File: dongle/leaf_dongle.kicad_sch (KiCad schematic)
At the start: 7 parts, among them J1 UP20-C-F-G-FL-P12-TR

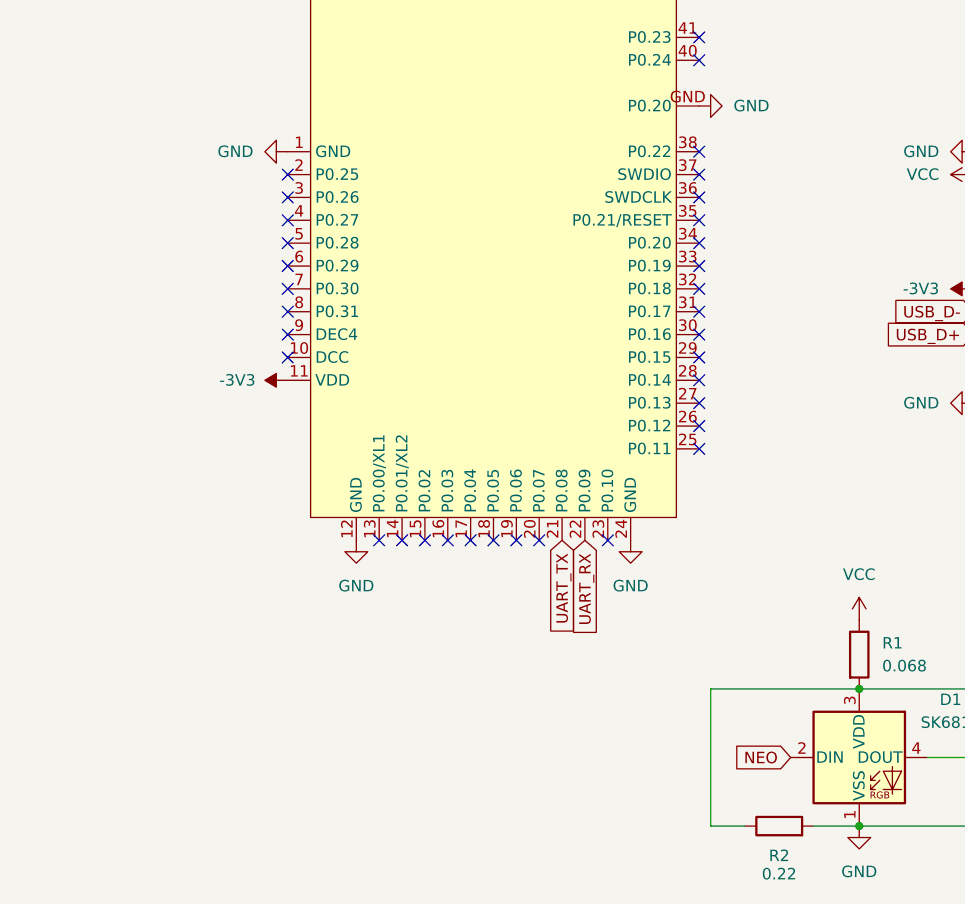
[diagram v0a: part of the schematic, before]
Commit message: Add TC-2030 interface; generate gerbers
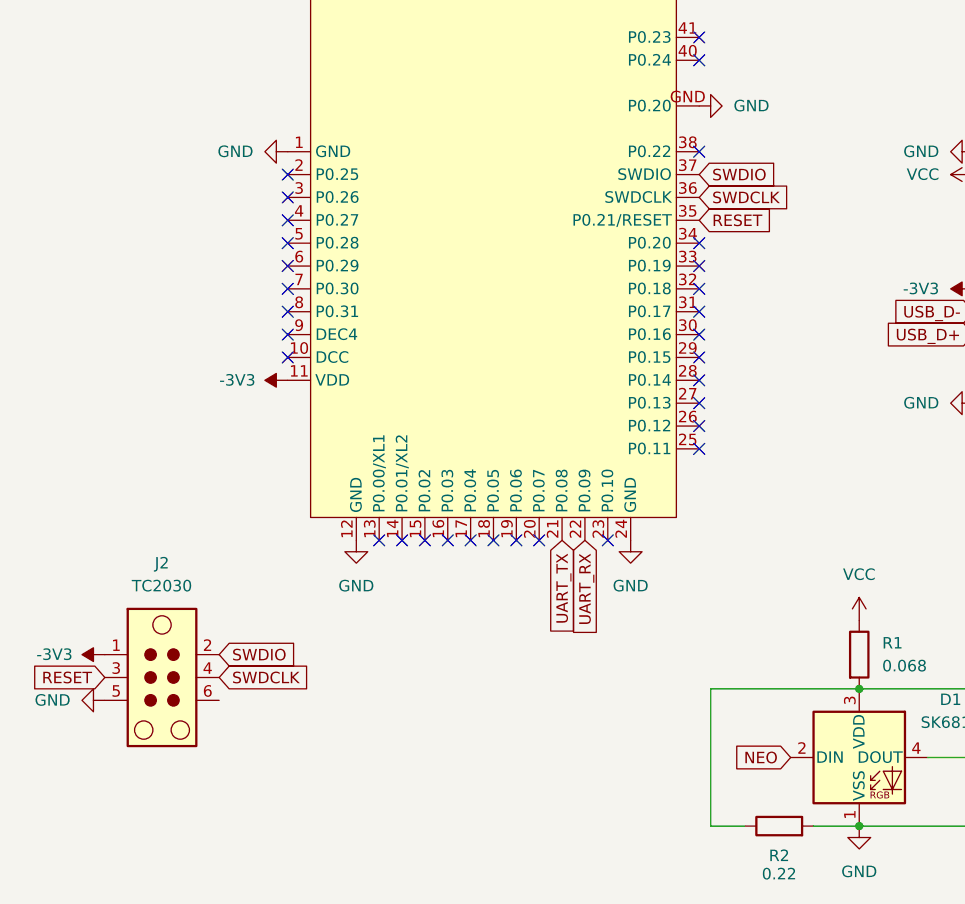
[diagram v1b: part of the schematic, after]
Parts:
- added J2: TC2030, Connector:Tag-Connect_TC2030-IDC-NL_2x03_P1.27mm_Vertical, symbol Connector:TC2030
- 1, U1: value ~ -> (none)
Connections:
- net -3V3: now also J2.1
- net GND: now also J2.5
- net RESET: now reaches U1.35 (P0.21/RESET)
- net RESET: now also J2.3
- net SWDCLK: now reaches U1.36 (SWDCLK)
- net SWDCLK: now also J2.4
- net SWDIO: now reaches U1.37 (SWDIO)
- net SWDIO: now also J2.2
- no-connect marks 63 -> 60

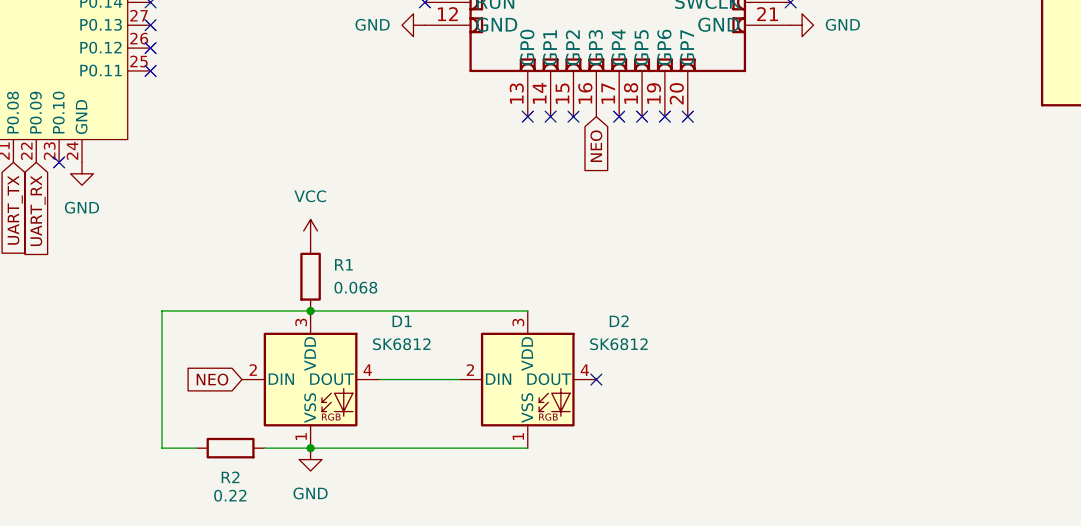
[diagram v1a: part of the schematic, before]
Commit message: Use logic shifter on dongle
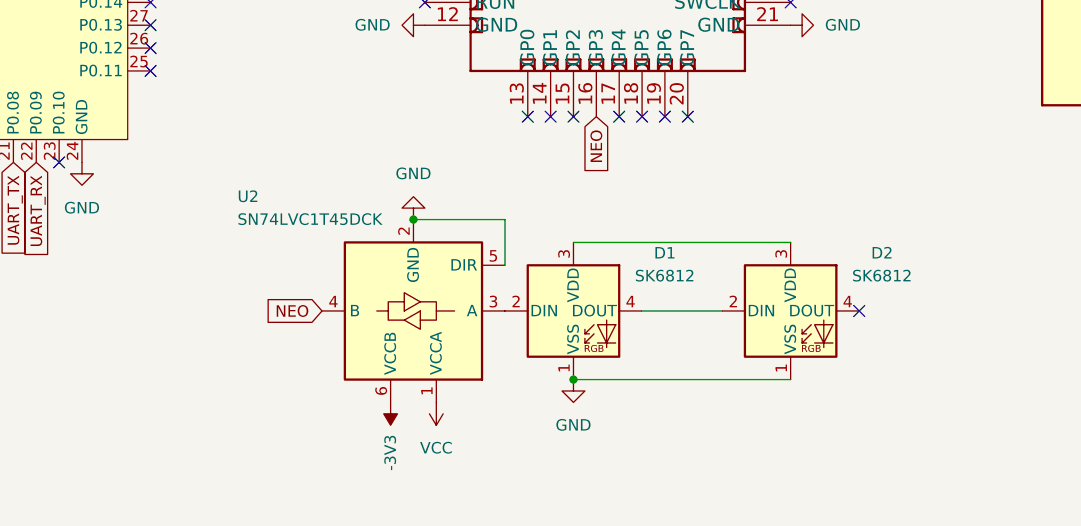
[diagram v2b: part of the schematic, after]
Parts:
- removed R1: 0.068, Resistor_SMD:R_0805_2012Metric, symbol Device:R
- removed R2: 0.22, Resistor_SMD:R_0805_2012Metric, symbol Device:R
- added U2: SN74LVC1T45DCK, Package_TO_SOT_SMD:SOT-363_SC-70-6, symbol Logic_LevelTranslator:SN74LVC1T45DCK
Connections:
- net -3V3: now also U2.6 (VCCB)
- net GND: now also U2.2 (GND), U2.5 (DIR)
- net NEO: now also U2.4 (B); no longer D1.2 (DIN)
- net VCC: now also U2.1 (VCCA)
- new net: D1.2 (DIN), U2.3 (A)
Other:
- moved on the sheet: D1, D2

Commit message: Update dongle to have 5.1k resistor for USB power
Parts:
- added R1: 5.1k, Resistor_SMD:R_0402_1005Metric, symbol Device:R
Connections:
- net GND: now also R1.2
- net at J1.A5 (CC1): now also R1.1
- no-connect marks 60 -> 59
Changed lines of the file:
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@@
 	)
 	(no_connect
-		(at 243.84 92.71)
-	)
-	(no_connect
 		(at 243.84 107.95)
 	)
@@
 	)
 	(symbol
+		(lib_id "Device:R")
+		(at 247.65 92.71 90)
+		(unit 1)
+		(body_style 1)
+		(exclude_from_sim no)
+		(in_bom yes)
+		(on_board yes)
+		(in_pos_files yes)
+		(dnp no)
+		(property "Reference" "R1"
+			(at 251.206 90.424 90)
+			(show_name no)
+			(do_not_autoplace no)
+			(effects
+				(font
+					(size 1.27 1.27)
+				)
+			)
+		)
+		(property "Value" "5.1k"
+			(at 255.524 90.424 90)
+			(show_name no)
+			(do_not_autoplace no)
+			(effects
+				(font
+					(size 1.27 1.27)
+				)
+			)
+		)
+		(property "Footprint" "Resistor_SMD:R_0402_1005Metric"
+			(at 247.65 94.488 90)
+			(hide yes)
+			(show_name no)
+			(do_not_autoplace no)
+			(effects
+				(font
+					(size 1.27 1.27)
+				)
+			)
+		)
+		(property "Datasheet" ""
+			(at 247.65 92.71 0)
+			(hide yes)
+			(show_name no)
+			(do_not_autoplace no)
+			(effects
+				(font
+					(size 1.27 1.27)
+				)
+			)
+		)
+		(property "Description" "Resistor"
+			(at 247.65 92.71 0)
+			(hide yes)
+			(show_name no)
+			(do_not_autoplace no)
+			(effects
+				(font
+					(size 1.27 1.27)
+				)
+			)
+		)
+		(pin "1"
+		)
+		(pin "2"
+		)
+		(instances
+			(project "leaf_dongle"
+				(path "/f6de454d-ae1c-4e0e-a2ba-a5d84f7bcb5c"
+					(reference "R1")
+					(unit 1)
+				)
+			)
+		)
+	)
+	(symbol
 		(lib_id "power:-3V3")
 		(at 58.42 132.08 90)
@@
 					(unit 1)
 				)
+			)
+		)
+	)
+	(symbol
+		(lib_id "power:GND")
+		(at 251.46 92.71 90)
+		(unit 1)
+		(body_style 1)
+		(exclude_from_sim no)
+		(in_bom yes)
+		(on_board yes)
+		(in_pos_files yes)
+		(dnp no)
+		(fields_autoplaced yes)
+		(property "Reference" "#PWR07"
+			(at 257.81 92.71 0)
+			(hide yes)
+			(show_name no)
+			(do_not_autoplace no)
+			(effects
+				(font
+					(size 1.27 1.27)
+				)
+			)
+		)
+		(property "Value" "GND"
+			(at 255.27 92.7099 90)
+			(show_name no)
+			(do_not_autoplace no)
+			(effects
+				(font
+					(size 1.27 1.27)
+				)
+				(justify right)
+			)
+		)
+		(property "Footprint" ""
+			(at 251.46 92.71 0)
+			(hide yes)
+			(show_name no)
+			(do_not_autoplace no)
+			(effects
+				(font
+					(size 1.27 1.27)
+				)
+			)
+		)
+		(property "Datasheet" ""
+			(at 251.46 92.71 0)
+			(hide yes)
+			(show_name no)
+			(do_not_autoplace no)
+			(effects
+				(font
+					(size 1.27 1.27)
+				)
+			)
+		)
+		(property "Description" "Power symbol creates a global label with name \"GND\" , ground"
+			(at 251.46 92.71 0)
+			(hide yes)
+			(show_name no)
+			(do_not_autoplace no)
+			(effects
+				(font
+					(size 1.27 1.27)
+				)
+			)
+		)
+		(pin "1"
+		)
+		(instances
+			(project "leaf_dongle"
+				(path "/f6de454d-ae1c-4e0e-a2ba-a5d84f7bcb5c"
+					(reference "#PWR07")
+					(unit 1)
+				)
